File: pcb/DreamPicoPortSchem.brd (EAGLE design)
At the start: 30 x 75 mm, 57 parts, among them J1 FFC3B07-20-T

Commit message: 177: Uploaded Rev 1.0 board files
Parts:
- removed C5: 35ZLH100MEFC6.3X11CAP_YX_6P3X11_RUB, 2025-03-29_20-35-50_Library:CAP_YX_6P3X11_RUB
- removed R29, R30, R31, R32, R33, R34, R35, R36: NP, Jumper Pad:RESC1005X40
- added C1: 35ZLH100MEFC6.3X11CAP_YX_6P3X11_RUB, 2025-03-29_20-35-50_Library:CAP_YX_6P3X11_RUB
- added JP10, JP11, JP12, JP5, JP6, JP7, JP8, JP9: JUMPER-SMT_2_NO_NO-SILK, SparkFun-Jumpers:SMT-JUMPER_2_NO_NO-SILK
- added R8: 120, Tinkercad:RESC1608X60
- moved 5V 12.7 mm to (26.2, 17.2)
- moved FAN 10.2 mm to (16.0, 17.2)
- moved 3.3V 7.62 mm to (23.6, 17.2)
- moved BAT 5.08 mm to (18.5, 17.2)
- moved GND 5.08 mm to (13.5, 17.2)
- moved RA3 4.96 mm to (11.0, 49.5), turned to 90 degrees
- moved RC3 4.93 mm to (16.8, 49.5), turned to 270 degrees
- moved CC 3.66 mm to (21.4, 56.3)
- moved UA 3.64 mm to (9.67, 56.3)
- moved UC 3.56 mm to (17.5, 56.3)
- moved RA5 3.55 mm to (8.58, 61.9), turned to 270 degrees
- moved CA 3.54 mm to (13.6, 56.3)
- moved RA6 3.54 mm to (11.0, 61.9)
- moved RA7 3.54 mm to (13.3, 61.9)
- moved RC5 3.54 mm to (16.7, 61.9)
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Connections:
- net +3.3V: now also R8.1
- net +5V: now also C1.1; no longer C5.1
- net GND: now also C1.2; no longer C5.2
- net N$11: now also JP10.1; no longer R34.2
- net N$13: now also JP8.2; no longer R32.1
- net N$15: now also JP7.2; no longer R31.1
- net N$17: now also R8.2
- net N$18: now also JP8.1; no longer R32.2
- net N$19: now also JP7.1; no longer R31.2
- net N$21: now also JP5.2; no longer R29.1
- net N$22: now also JP9.1; no longer R33.2
- net N$25: now also JP10.2; no longer R34.1
- net N$26: now also JP9.2; no longer R33.1
- net N$29: now also JP12.1; no longer R36.2
- net N$3: now also JP6.2; no longer R30.1
- net N$30: now also JP11.1; no longer R35.2
- net N$36: now also JP12.2; no longer R36.1
- net N$37: now also JP11.2; no longer R35.1
- net N$6: now also JP5.1; no longer R29.2
- net N$7: now also JP6.1; no longer R30.2
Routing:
- net N$23: track 47.7 -> 6.99 mm, vias 2 -> 0
- net N$6: track 54.8 -> 91.9 mm, vias 2 -> 0
- net N$29: track 17.5 -> 37.8 mm
- net C-B: track 20.4 -> 40.2 mm
- net N$19: track 44.3 -> 27.5 mm
- net N$37: track 46.0 -> 29.9 mm
- net N$10: track 26.5 -> 41.4 mm, vias 2 -> 1
- net N$1: track 25.1 -> 11.3 mm, vias 1 -> 0
- net GND: track 276.8 -> 290.0 mm, vias 3 -> 2
- net N$3: track 26.8 -> 39.0 mm, vias 2 -> 1
- net +3.3V: track 154.4 -> 143.4 mm, vias 3 -> 8
- net N$8: track 29.6 -> 20.3 mm, vias 2 -> 0
- net D-A: track 25.2 -> 34.5 mm, vias 1 -> 0
- net N$26: track 68.8 -> 60.0 mm, vias 6 -> 2
- net N$25: track 56.9 -> 49.6 mm
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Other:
- board text added: "C1"
- board text added: "Rev 1.0"
- board text removed: "Rev 0.2"

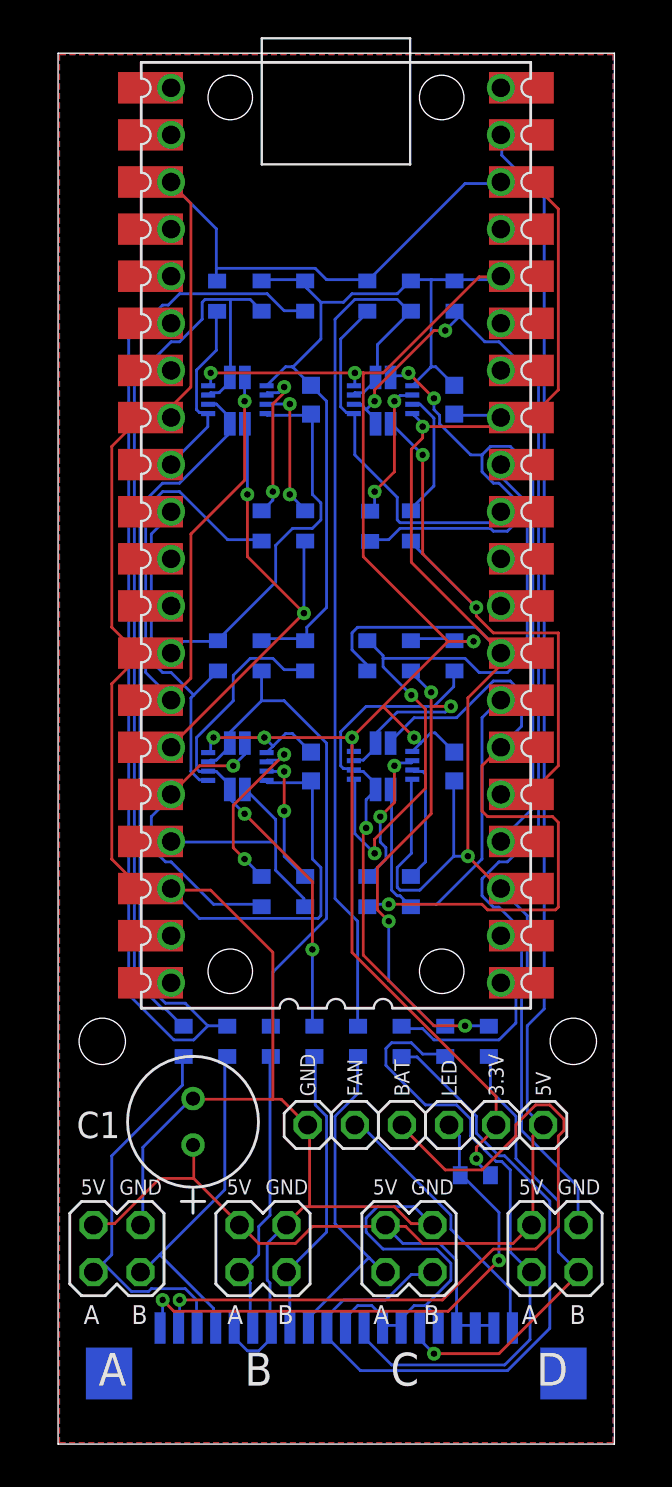
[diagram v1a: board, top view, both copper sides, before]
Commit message: 177: Changed R[A-D]1 and R[A-D]2 resistors to 1206 size
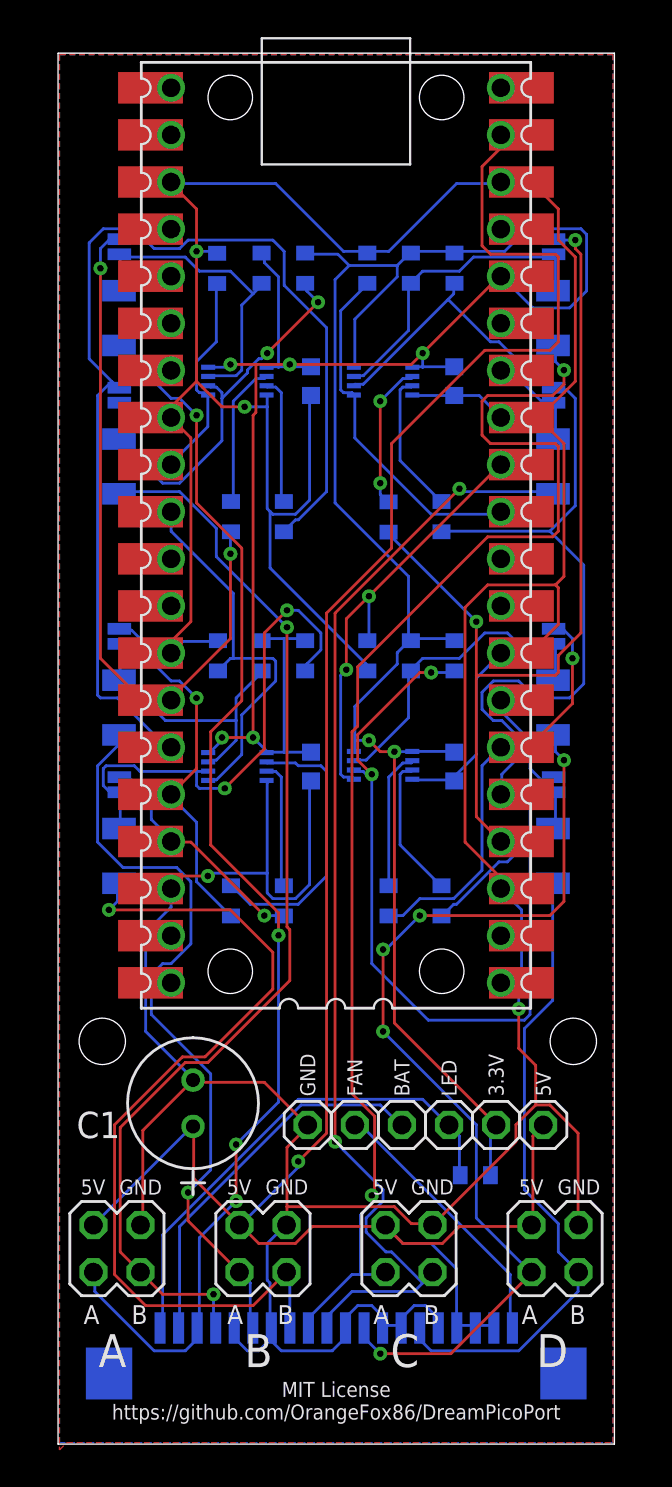
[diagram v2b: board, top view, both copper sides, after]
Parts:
- RA1, RA2, RB1, RB2, RC1, RC2, RD1, RD2: device Tinkercad:RESC1608X60 -> Resistor:RESC3216X70
- moved RC1 40.4 mm to (26.7, 60.7)
- moved RA1 39.2 mm to (3.29, 60.7)
- moved RC2 32.1 mm to (26.7, 52.7)
- moved RA2 31.5 mm to (3.29, 52.7)
- moved RB1 19.8 mm to (3.29, 39.7)
- moved RD1 18.9 mm to (26.7, 39.7)
- moved RB2 14.5 mm to (3.29, 31.7)
- moved JP10 11.6 mm to (26.7, 64.6), turned to 270 degrees
- moved JP12 10.8 mm to (26.7, 43.6), turned to 270 degrees
- moved RD2 10.6 mm to (26.7, 31.7)
- moved JP6 9.50 mm to (3.31, 64.6), turned to 90 degrees
- moved JP9 9.32 mm to (26.7, 56.6), turned to 270 degrees
- moved JP11 9.20 mm to (26.7, 35.6), turned to 270 degrees
- moved JP8 8.58 mm to (3.31, 43.6), turned to 90 degrees
- moved JP5 6.55 mm to (3.31, 56.6), turned to 90 degrees
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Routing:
- net N$6: track 91.9 -> 21.7 mm, vias 0 -> 2
- net C-A: track 18.5 -> 71.2 mm, vias 0 -> 2
- net A-A: track 21.9 -> 68.8 mm, vias 0 -> 4
- net N$26: track 60.0 -> 18.7 mm, vias 2 -> 0
- net A-B: track 18.9 -> 59.1 mm, vias 0 -> 2
- net N$7: track 51.5 -> 17.2 mm
- net N$21: track 27.9 -> 61.0 mm, vias 2 -> 0
- net N$25: track 49.6 -> 17.0 mm
- net B-B: track 15.9 -> 46.9 mm, vias 0 -> 1
- net B-A: track 15.7 -> 40.7 mm, vias 0 -> 1
- net C-B: track 40.2 -> 61.0 mm, vias 0 -> 2
- net N$10: track 41.4 -> 20.6 mm, vias 1 -> 0
- net +5V: track 101.7 -> 120.6 mm, vias 0 -> 1
- net +3.3V: track 143.4 -> 162.1 mm, vias 8 -> 7
- net D-A: track 34.5 -> 52.6 mm, vias 0 -> 5
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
